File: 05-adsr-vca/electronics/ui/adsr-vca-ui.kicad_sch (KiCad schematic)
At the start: 28 parts, among them J1 Conn_02x03_Odd_Even, J3 Conn_02x03_Odd_Even, J4 Conn_01x02, J5 Conn_01x06, J6 Conn_02x03_Odd_Even, J8 Conn_02x03_Odd_Even, Q1 2N3904, Q2 2N3906

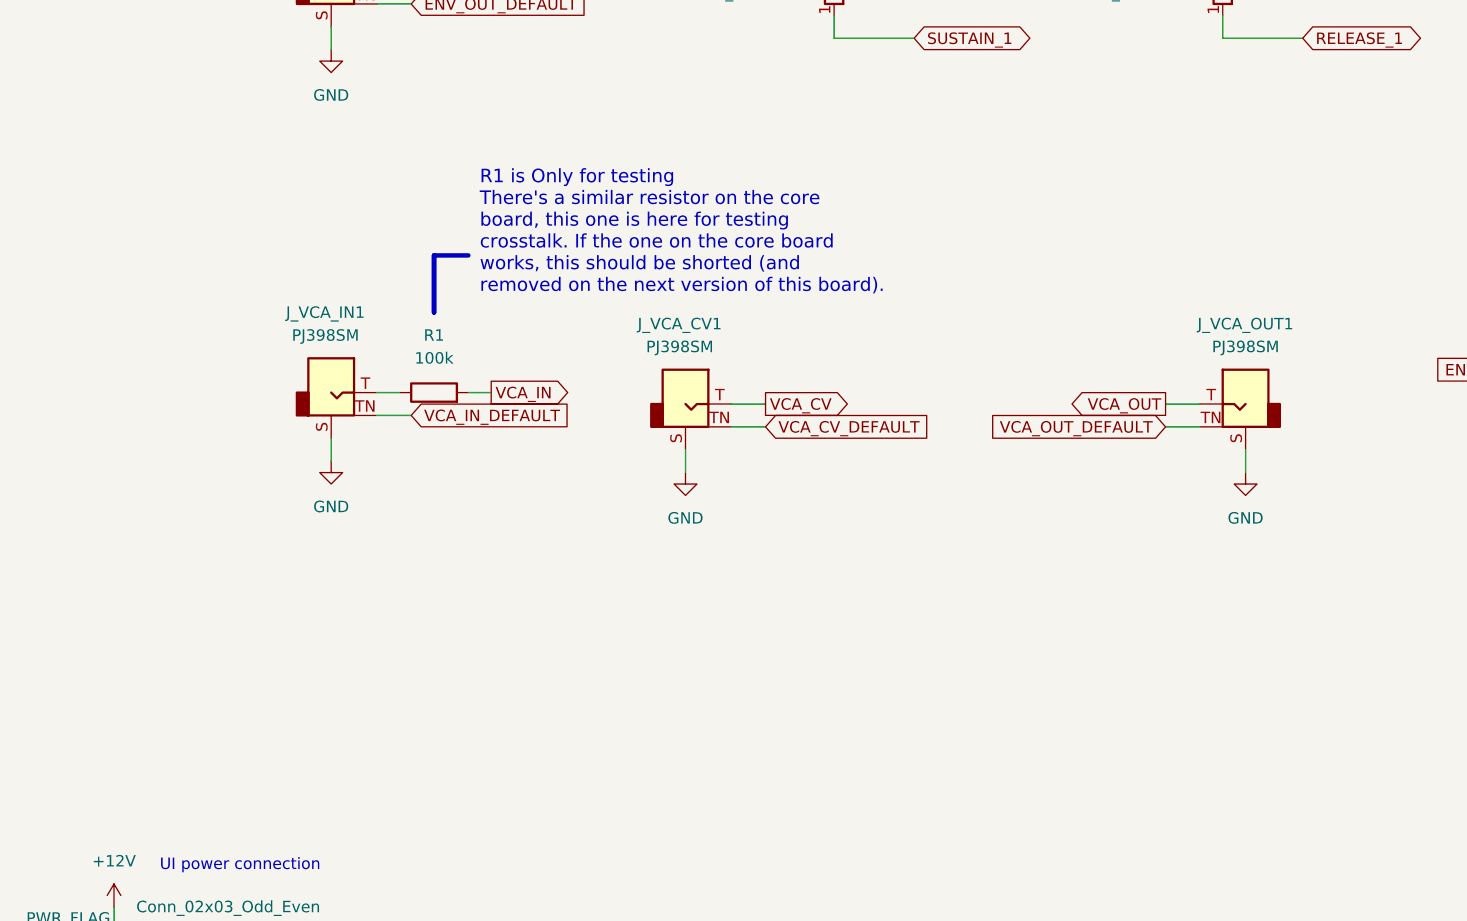
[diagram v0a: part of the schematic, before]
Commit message: Added VCA amp bias pot
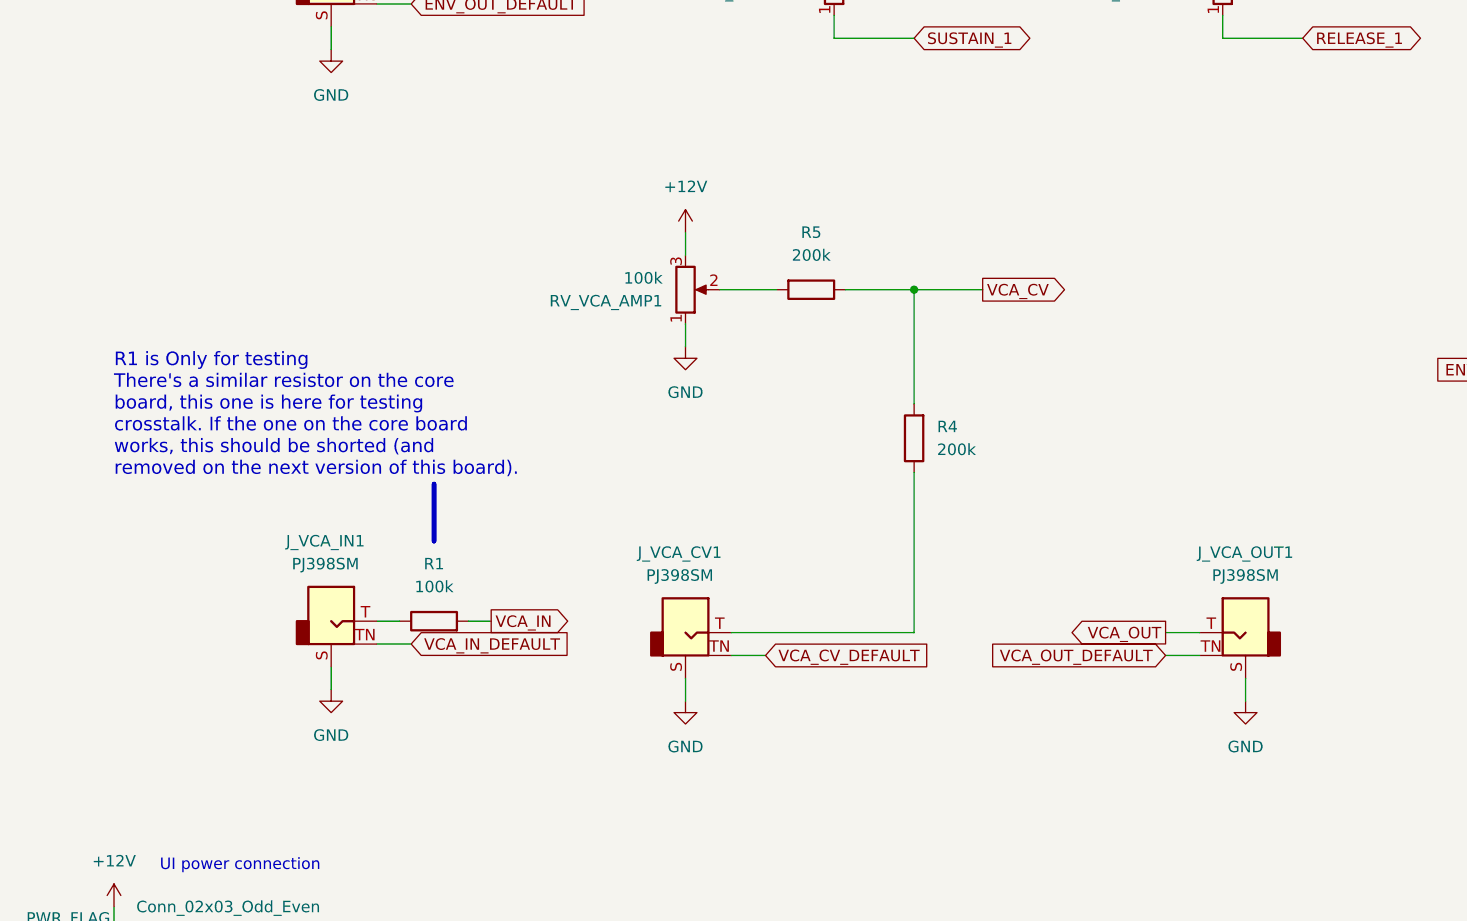
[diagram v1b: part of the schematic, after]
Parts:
- added R4, R5: 200k, Shmoergh_Custom_Footprints:R_Axial_DIN0207_L6.3mm_D2.5mm_P7.62mm_Horizontal, symbol Device:R
- added RV_VCA_AMP1: 100k, Shmoergh_Custom_Footprints:Potentiometer_Bourns_Single-PTV09A, symbol Device:R_Potentiometer
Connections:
- net +12V: now also RV_VCA_AMP1.3
- net GND: now also RV_VCA_AMP1.1
- net VCA_CV: now also R4.2, R5.1; no longer J_VCA_CV1.T
- new net: J_VCA_CV1.T, R4.1
- new net: R5.2, RV_VCA_AMP1.2
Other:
- moved on the sheet: J_VCA_CV1, J_VCA_IN1, J_VCA_OUT1, R1

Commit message: Reverted VCA to no-bias version
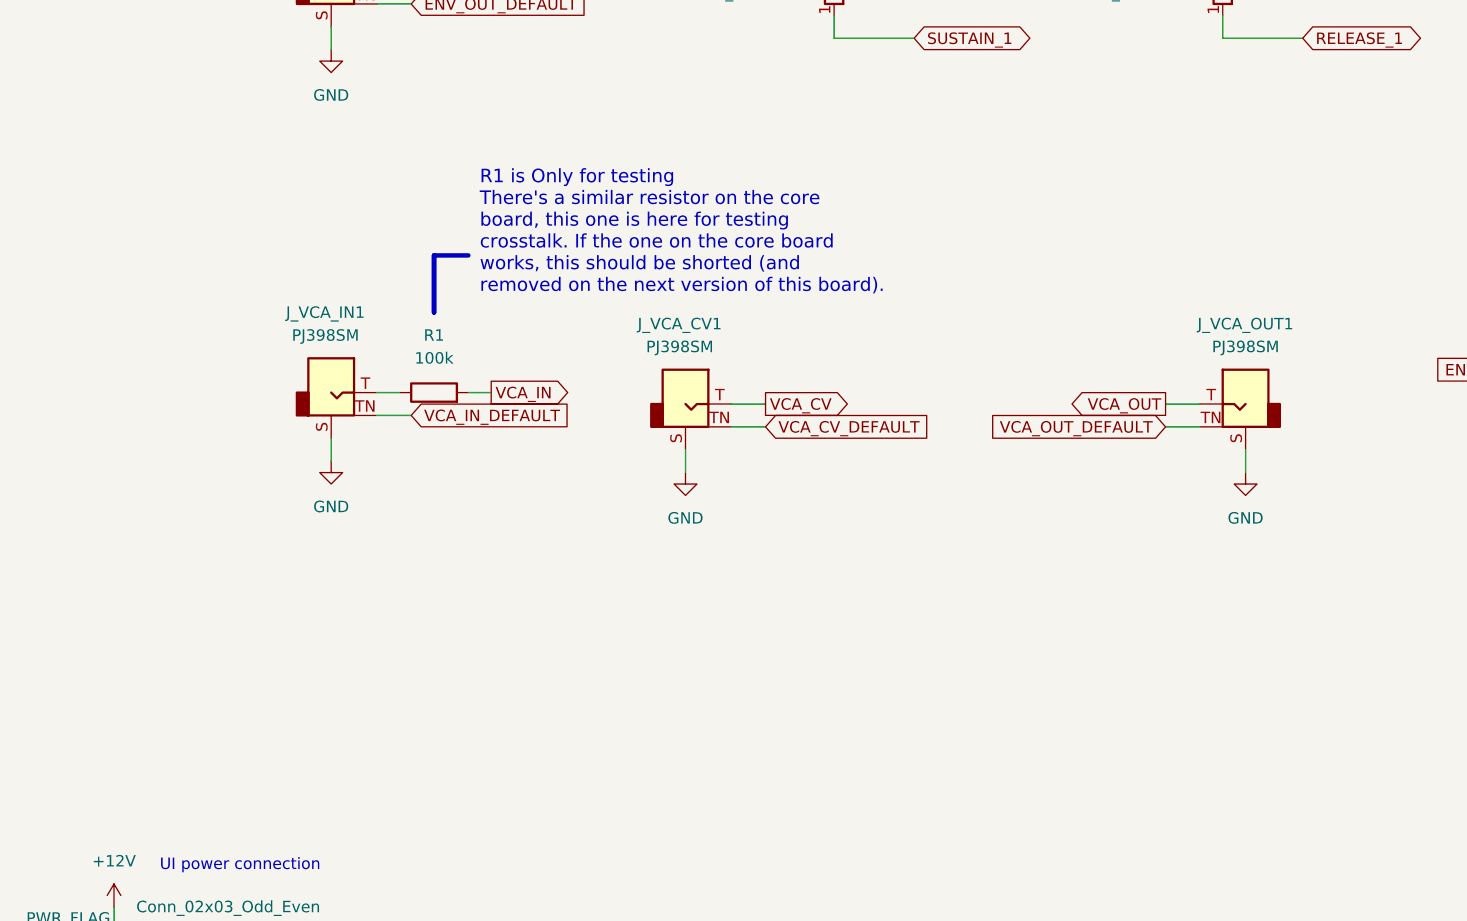
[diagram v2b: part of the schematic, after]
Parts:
- removed R4, R5: 200k, Shmoergh_Custom_Footprints:R_Axial_DIN0207_L6.3mm_D2.5mm_P7.62mm_Horizontal, symbol Device:R
- removed RV_VCA_AMP1: 100k, Shmoergh_Custom_Footprints:Potentiometer_Bourns_Single-PTV09A, symbol Device:R_Potentiometer
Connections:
- net VCA_CV: now also J_VCA_CV1.T
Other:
- moved on the sheet: J_VCA_CV1, J_VCA_IN1, J_VCA_OUT1, R1
